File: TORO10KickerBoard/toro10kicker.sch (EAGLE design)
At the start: 94 parts, among them CN2 43650-0800, CN3 ARM-JTAG, CN4 5569-04A2, CN5 5569-02A2, CN6 5569-02A2, Q1 BSS138, Q2 BSS138, Q3 CSD19538Q3A, Q4 BSS138, U1 NJM7812S, U2 NJM7805S, U3 SAMC21E18A-A, U4 LT3751EUFD, U5 INA181A1IDBV, U6 UCC27524DGN

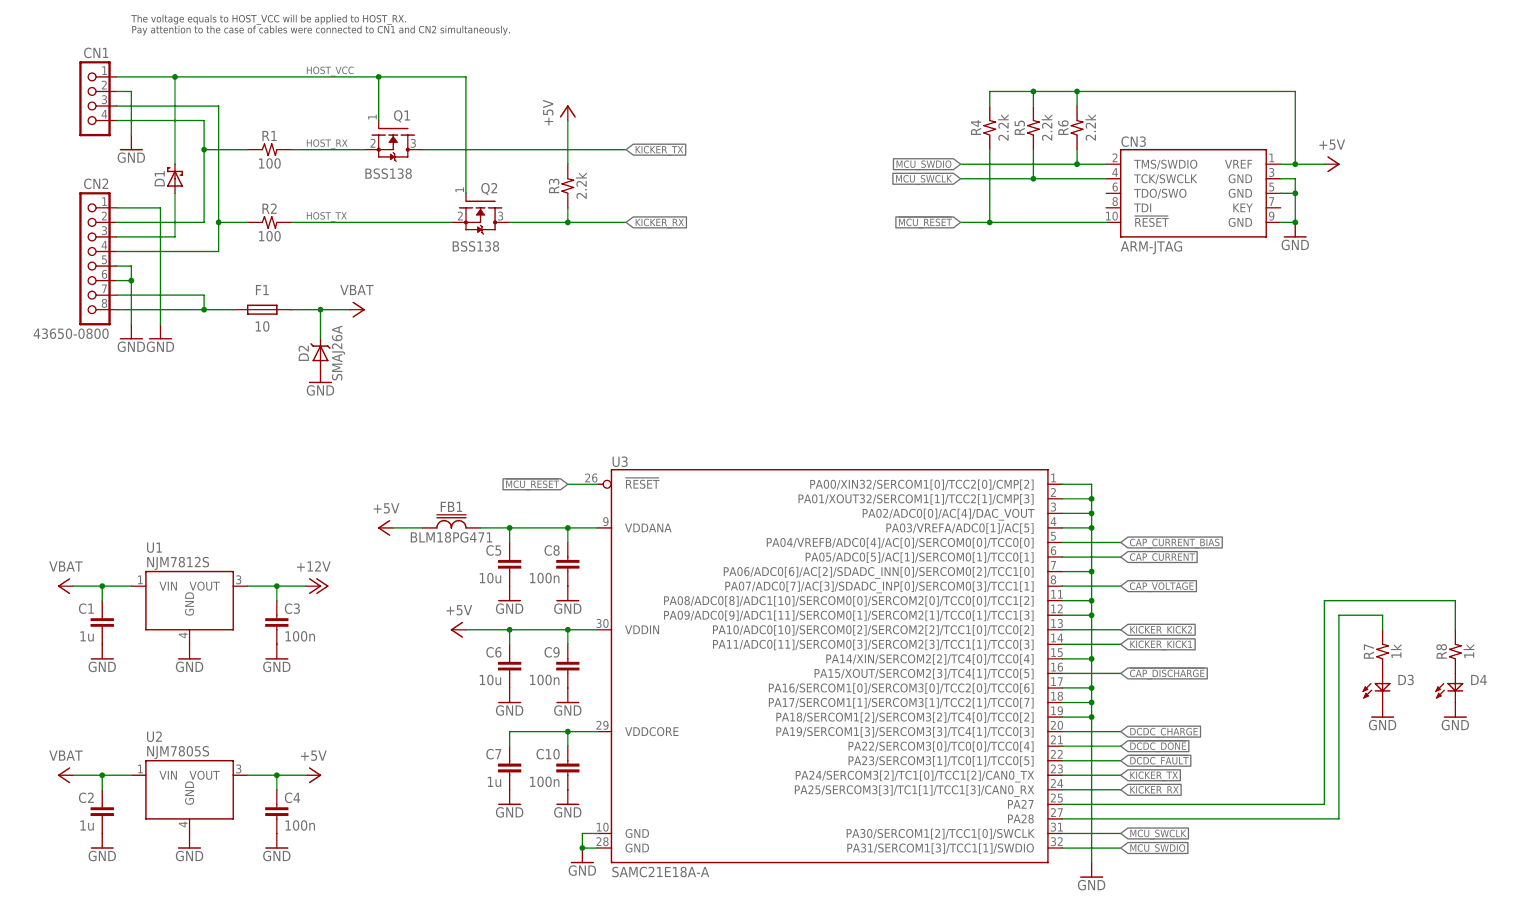
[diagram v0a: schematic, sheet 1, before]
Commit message: add kicker BOM
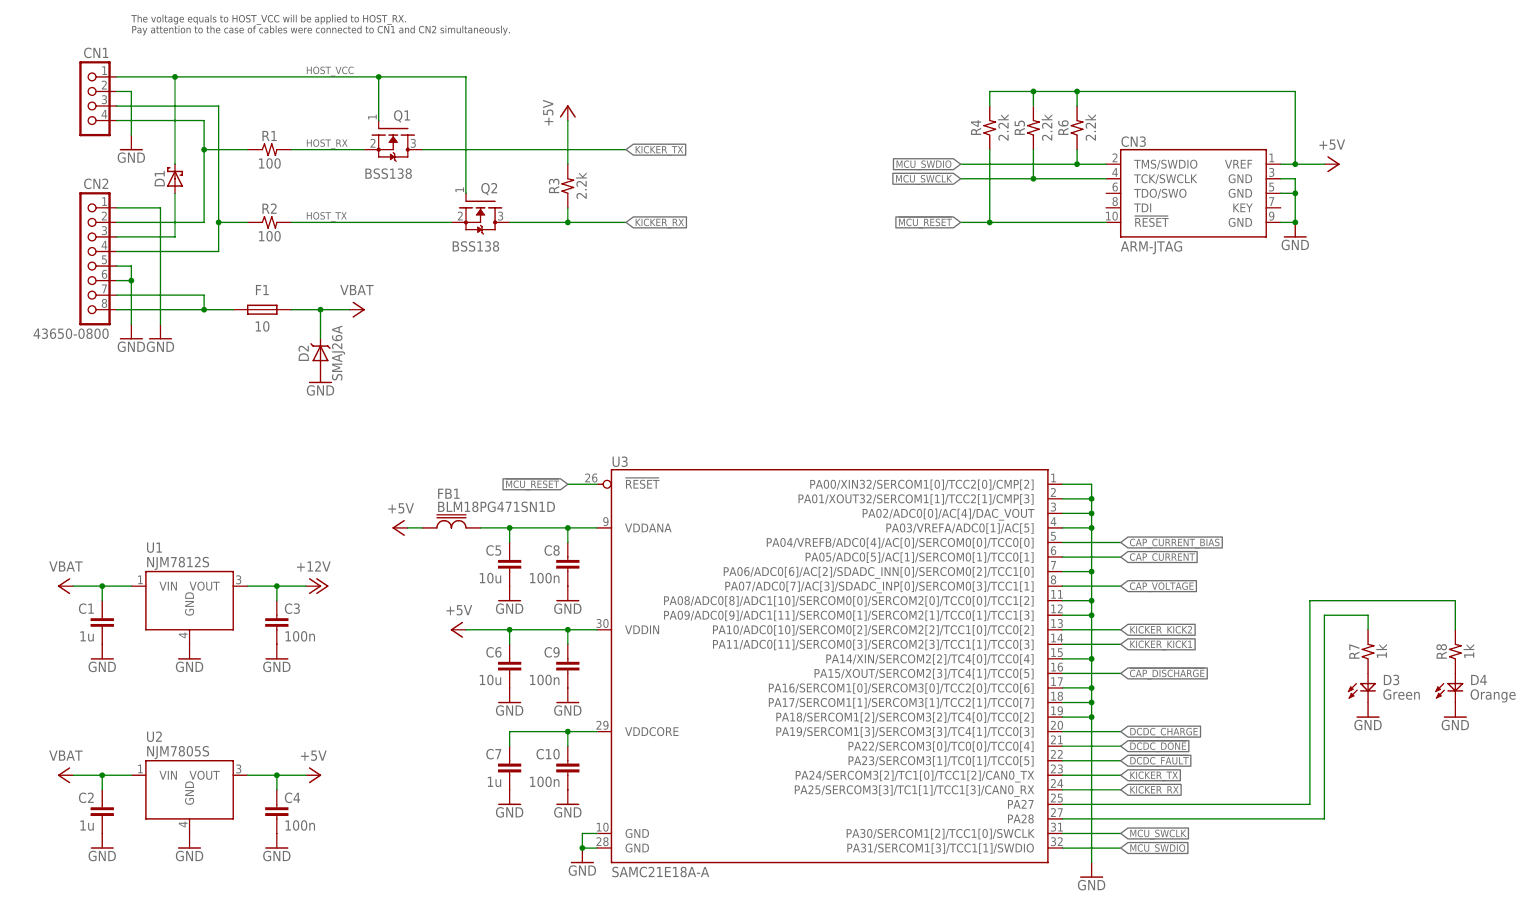
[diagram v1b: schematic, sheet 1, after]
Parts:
- removed VR1: TC33X-2-501E, kiks-passive:VR-TC33X
- added R40: 10, kiks-passive:R2012
- D3: value (none) -> Green
- D4: value (none) -> Orange
- FB1: value BLM18PG471 -> BLM18PG471SN1D
- Q5: value (none) -> BSP130
- R23: value 10k -> TC33X-2-501E; device kiks-passive:R1608 -> kiks-passive:VR-TC33X
- R25: value WSL4026L3000FEB -> 10k; device kiks-passive:WSL4026 -> kiks-passive:R1608
- R26: value 10k -> WSL4026L3000FEB; device kiks-passive:R1608 -> kiks-passive:WSL4026
- R27: value 1k -> 10k
- R28: value 100k -> 1k; device kiks-passive:R3216 -> kiks-passive:R1608
- R30: value 1M -> 100k
- R31: value PFS35-1KF1 -> 1M; device kiks-passive:PFS35 -> kiks-passive:R3216
- R32: value 4.7k -> PFS35-1KF1; device kiks-passive:R1608 -> kiks-passive:PFS35
- R34: value DNC -> 4.7k
- R36: value 10 -> DNC; device kiks-passive:R2012 -> kiks-passive:R1608
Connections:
- net !CAP_DISCHARGE: now also R27.2, R28.1; no longer R26.2, R27.1
- net +5V: now also R24.2; no longer R23.2
- net CAP_CURRENT_BIAS: now also R24.1, R25.2; no longer R23.1, R24.2
- net GND: now also R23.A, R23.W, R25.1, R26.1A, R27.1, R32.S, R36.1; no longer R24.1, R25.1A, R26.1, R31.S, R32.1, VR1.A, VR1.W
- net KICKER_KICK1: now also R33.2; no longer R32.2
- net KICKER_KICK2: now also R34.2; no longer R33.2
- net N$14: now also R23.B; no longer VR1.B
- net N$19: now also R26.2A; no longer R25.2A
- net N$21: now also R29.1, R30.2; no longer R28.1, R29.2
- net N$23: now also R37.2; no longer R36.2
- net N$24: now also R38.2; no longer R37.2
- net N$25: now also R35.2, R38.1; no longer R34.2, R36.1
- net N$26: now also R39.2; no longer R38.2
- net N$27: now also R40.2; no longer R39.2
- net N$28: now also R36.2, R40.1; no longer R35.2, R38.1
- net N$30: now also R31.1; no longer R30.1
- net N$32: now also R28.2; no longer R27.2
- net N$33: now also R30.1; no longer R29.1
- net N$36: now also R26.2B; no longer R25.2B
- net N$37: now also R26.1B; no longer R25.1B
- net N$8: now also R31.2, R32.1; no longer R30.2, R31.1
- net VCAP: now also R29.2, R32.2; no longer R28.2, R31.2
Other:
- moved on the sheet: D3, R24, R27, R28, R29, R30, R33, R34, R35, R36, R37, R38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
